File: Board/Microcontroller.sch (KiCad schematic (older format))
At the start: 12 parts, among them U2 ATxmega16A4U-AU, U3 LM2936-3.3, Y1 Crystal

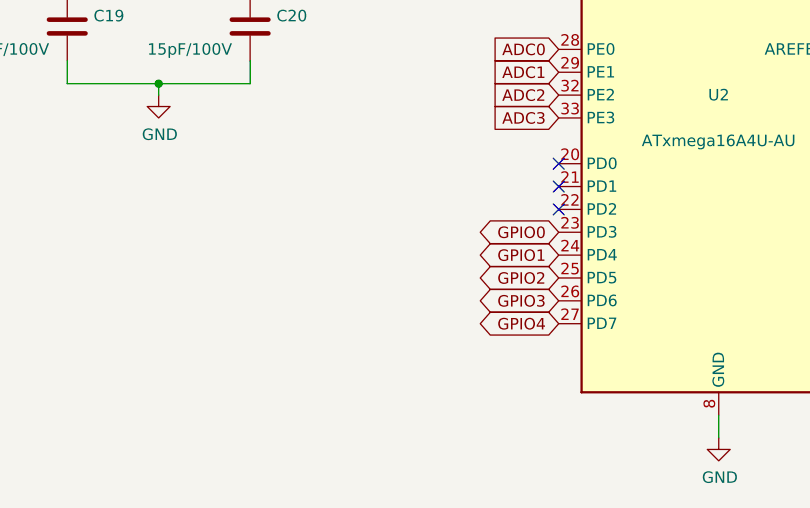
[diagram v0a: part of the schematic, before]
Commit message: Added protection resistors on xmega GPIOs. Corrected prog connector outline.
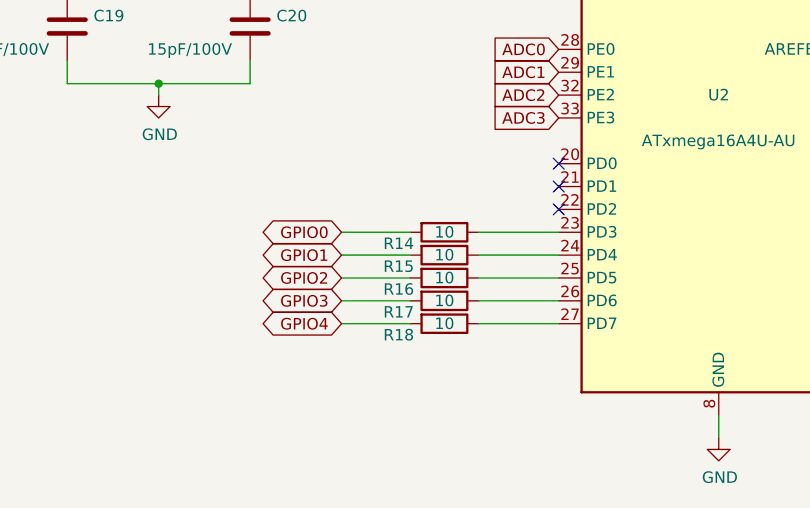
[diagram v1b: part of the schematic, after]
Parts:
- added R14, R15, R16, R17, R18: 10, Resistor_SMD:R_0603_1608Metric_Pad1.05x0.95mm_HandSolder, symbol Device:R
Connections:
- net GPIO0: now also R14.2; no longer U2.23 (PD3)
- net GPIO1: now also R15.2; no longer U2.24 (PD4)
- net GPIO2: now also R16.2; no longer U2.25 (PD5)
- net GPIO3: now also R17.2; no longer U2.26 (PD6)
- net GPIO4: now also R18.2; no longer U2.27 (PD7)
- new net: R14.1, U2.23 (PD3)
- new net: R15.1, U2.24 (PD4)
- new net: R16.1, U2.25 (PD5)
- new net: R17.1, U2.26 (PD6)
- new net: R18.1, U2.27 (PD7)
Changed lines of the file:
@@
 Text GLabel 3050 2200 1    50   Input ~ 0
 PDI_CLK
-Text GLabel 3250 4050 0    50   BiDi ~ 0
+Text GLabel 2300 4050 0    50   BiDi ~ 0
 GPIO0
-Text GLabel 3250 4150 0    50   BiDi ~ 0
+Text GLabel 2300 4150 0    50   BiDi ~ 0
 GPIO1
-Text GLabel 3250 4250 0    50   BiDi ~ 0
+Text GLabel 2300 4250 0    50   BiDi ~ 0
 GPIO2
-Text GLabel 3250 4350 0    50   BiDi ~ 0
+Text GLabel 2300 4350 0    50   BiDi ~ 0
 GPIO3
-Text GLabel 3250 4450 0    50   BiDi ~ 0
+Text GLabel 2300 4450 0    50   BiDi ~ 0
 GPIO4
 NoConn ~ 3250 3750
@@
 	1    0    0    -1
 $EndComp
+$Comp
+L Device:R R14
+U 1 1 5C0E896F
+P 2750 4050
+F 0 "R14" V 2800 3850 50  0000 C CNN
+F 1 "10" V 2750 4050 50  0000 C CNN
+F 2 "Resistor_SMD:R_0603_1608Metric_Pad1.05x0.95mm_HandSolder" V 2680 4050 50  0001 C CNN
+F 3 "~" H 2750 4050 50  0001 C CNN
+	1    2750 4050
+	0    1    1    0
+$EndComp
+$Comp
+L Device:R R15
+U 1 1 5C0E8A96
+P 2750 4150
+F 0 "R15" V 2800 3950 50  0000 C CNN
+F 1 "10" V 2750 4150 50  0000 C CNN
+F 2 "Resistor_SMD:R_0603_1608Metric_Pad1.05x0.95mm_HandSolder" V 2680 4150 50  0001 C CNN
+F 3 "~" H 2750 4150 50  0001 C CNN
+	1    2750 4150
+	0    1    1    0
+$EndComp
+$Comp
+L Device:R R16
+U 1 1 5C0E8AC6
+P 2750 4250
+F 0 "R16" V 2800 4050 50  0000 C CNN
+F 1 "10" V 2750 4250 50  0000 C CNN
+F 2 "Resistor_SMD:R_0603_1608Metric_Pad1.05x0.95mm_HandSolder" V 2680 4250 50  0001 C CNN
+F 3 "~" H 2750 4250 50  0001 C CNN
+	1    2750 4250
+	0    1    1    0
+$EndComp
+$Comp
+L Device:R R17
+U 1 1 5C0E8AF8
+P 2750 4350
+F 0 "R17" V 2800 4150 50  0000 C CNN
+F 1 "10" V 2750 4350 50  0000 C CNN
+F 2 "Resistor_SMD:R_0603_1608Metric_Pad1.05x0.95mm_HandSolder" V 2680 4350 50  0001 C CNN
+F 3 "~" H 2750 4350 50  0001 C CNN
+	1    2750 4350
+	0    1    1    0
+$EndComp
+$Comp
+L Device:R R18
+U 1 1 5C0E8B2C
+P 2750 4450
+F 0 "R18" V 2800 4250 50  0000 C CNN
+F 1 "10" V 2750 4450 50  0000 C CNN
+F 2 "Resistor_SMD:R_0603_1608Metric_Pad1.05x0.95mm_HandSolder" V 2680 4450 50  0001 C CNN
+F 3 "~" H 2750 4450 50  0001 C CNN
+	1    2750 4450
+	0    1    1    0
+$EndComp
+Wire Wire Line
+	3250 4050 2900 4050
+Wire Wire Line
+	2900 4150 3250 4150
+Wire Wire Line
+	2900 4250 3250 4250
+Wire Wire Line
+	2900 4350 3250 4350
+Wire Wire Line
+	2900 4450 3250 4450
+Wire Wire Line
+	2600 4050 2300 4050
+Wire Wire Line
+	2600 4150 2300 4150
+Wire Wire Line
+	2300 4250 2600 4250
+Wire Wire Line
+	2300 4350 2600 4350
+Wire Wire Line
+	2300 4450 2600 4450
 $EndSCHEMATC

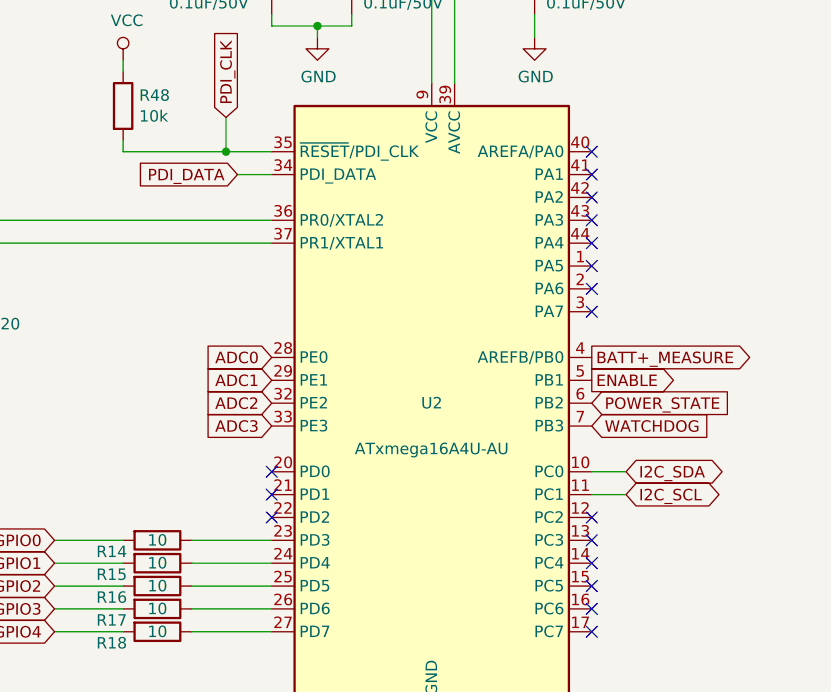
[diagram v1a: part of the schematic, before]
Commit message: MAJOR CORRECTION: moved ADCs to correct port on xmega. Added a LED controlled by the xmega.
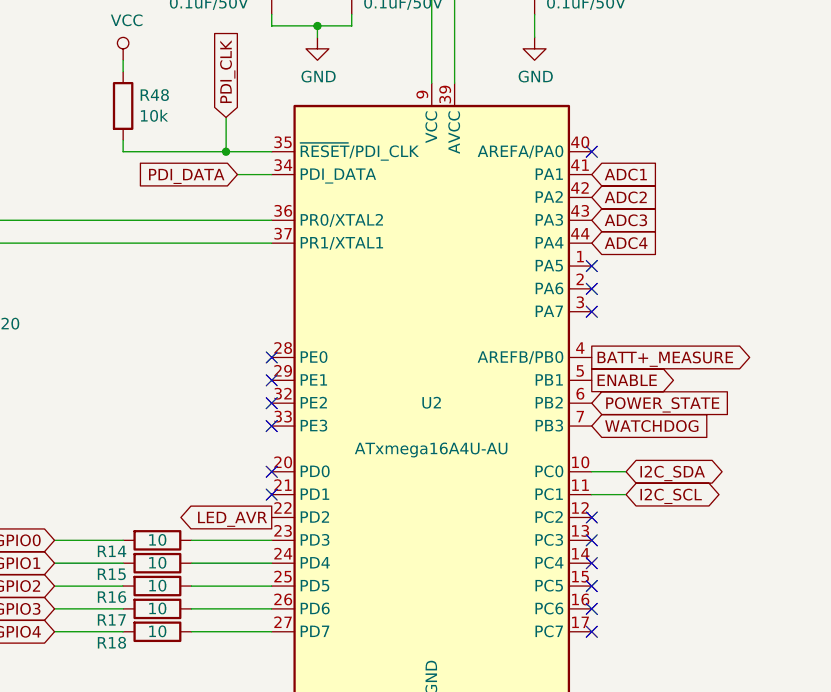
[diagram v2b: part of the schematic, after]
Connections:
- net ADC1: now also U2.41 (PA1); no longer U2.29 (PE1)
- net ADC2: now also U2.42 (PA2); no longer U2.32 (PE2)
- net ADC3: now also U2.43 (PA3); no longer U2.33 (PE3)
- net LED_AVR: now reaches U2.22 (PD2)
- net ADC4: now reaches U2.44 (PA4)
- net ADC0: no longer names the net of U2.28 (PE0)
- no-connect marks 17 -> 16
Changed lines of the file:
@@
 Text GLabel 4650 3550 2    50   Input ~ 0
 WATCHDOG
-Text GLabel 3250 3250 0    50   Input ~ 0
-ADC0
-Text GLabel 3250 3350 0    50   Input ~ 0
-ADC1
-Text GLabel 3250 3450 0    50   Input ~ 0
+Text GLabel 4650 2550 2    50   Input ~ 0
 ADC2
-Text GLabel 3250 3550 0    50   Input ~ 0
+Text GLabel 4650 2650 2    50   Input ~ 0
 ADC3
 Text GLabel 4800 3750 2    50   BiDi ~ 0
@@
 Wire Wire Line
 	4200 1400 4400 1400
-NoConn ~ 4650 2750
 NoConn ~ 4650 2850
 NoConn ~ 4650 2950
-NoConn ~ 4650 3050
 NoConn ~ 4650 3950
 NoConn ~ 4650 4050
@@
 NoConn ~ 3250 3750
 NoConn ~ 3250 3850
-NoConn ~ 3250 3950
-NoConn ~ 4650 2350
-NoConn ~ 4650 2450
-NoConn ~ 4650 2550
-NoConn ~ 4650 2650
 $Comp
 L power_custom:LM2936-3.3 U3
@@
 Wire Wire Line
 	2300 4450 2600 4450
+NoConn ~ 4650 3050
+Text GLabel 4650 2450 2    50   Input ~ 0
+ADC1
+NoConn ~ 3250 3250
+NoConn ~ 3250 3350
+NoConn ~ 3250 3450
+NoConn ~ 3250 3550
+Text GLabel 4650 2750 2    50   Input ~ 0
+ADC4
+NoConn ~ 4650 2350
+Text GLabel 3250 3950 0    50   Output ~ 0
+LED_AVR
 $EndSCHEMATC
